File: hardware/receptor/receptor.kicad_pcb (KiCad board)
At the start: 2 copper layers, 100 x 76 mm, 48 parts, among them J1 I2C, J2 USB-C, J3 5V EXT, J4 BOBINA 5V, Q1 AO3400A, SW1 RESET, SW2 BOOT, U1 ESP32-C3-MINI-1-H4X, U2 E220-900T30D, U4 USBLC6-2SC6, U5 AP2112K-3.3

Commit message: feat(hw): layout compacto de 86x52 mm nas duas placas
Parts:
- removed H3, H4: MountingHole_3.2mm_M3, MountingHole:MountingHole_3.2mm_M3
- moved R11 73.0 mm to (80.2, 27.8)
- moved F1 51.6 mm to (75.6, 28.2)
- moved J2 48.7 mm to (14.0, 47.8), turned to 0 degrees
- moved H2 46.5 mm to (82.5, 48.5)
- moved H1 44.5 mm to (3.50, 48.5)
- moved D3 41.4 mm to (68.9, 28.8)
- moved R12 38.3 mm to (45.5, 37.7)
- moved R6 34.0 mm to (30.6, 4.12)
- moved R5 33.9 mm to (26.7, 4.12)
- moved R4 33.8 mm to (22.9, 4.12)
- moved R3 33.6 mm to (19.0, 4.12)
- moved D4 32.4 mm to (60.9, 29.3)
- moved J3 30.6 mm to (48.0, 46.4)
- moved U1 30.4 mm to (11.1, 7.60)
- moved C7 30.2 mm to (30.9, 35.2)
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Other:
- board size 100 x 76 mm -> 86 x 52 mm
- board text added: "ENTRADA 5V APENAS"
- board text added: "FECHADO=BOMBA"
- board text added: "J3: 5V+ | GND"
- board text added: "J4: BOBINA 5V+ | -"
- board text added: "JP1 PAPEL:"
- board text added: "NAO LIGAR 12V"
- board text added: "NAO LIGAR O E220"
- board text added: "RECEPTOR"
- board text added: "SEM ANTENA!"
- board text removed: "BOBINA 5V: + | -"
- board text removed: "ENTRADA 5V APENAS - NAO LIGAR 12V"
- board text removed: "JP1 PAPEL: FECHADO=BOMBA"
- board text removed: "NAO LIGAR O E220 SEM ANTENA!"
- board text removed: "O E220 TRANSMITE NO BOOT"
- board text removed: "RECEPTOR (BOMBA)"

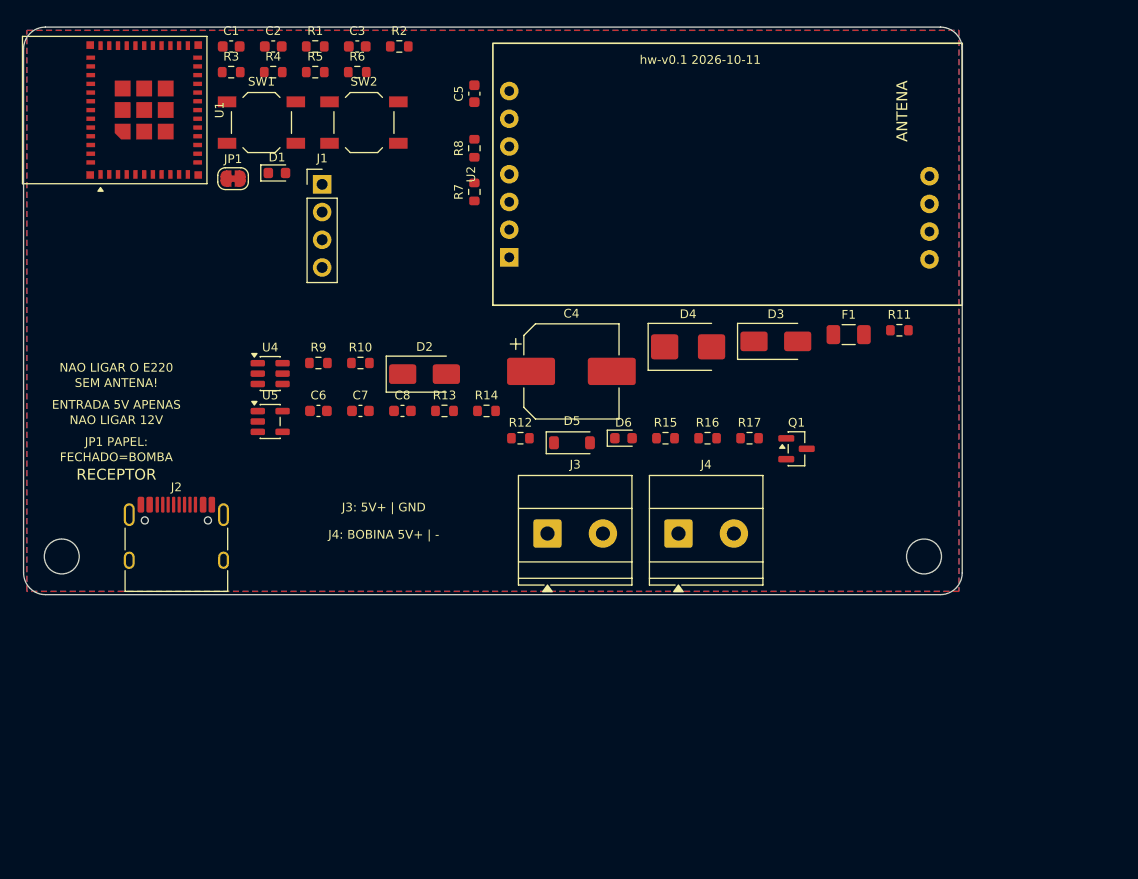
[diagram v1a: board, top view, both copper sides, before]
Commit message: wip(hw): roteador proprio, layout v2 com pecas sob o E220 (checkpoint antes de trocar para jack 12 V)
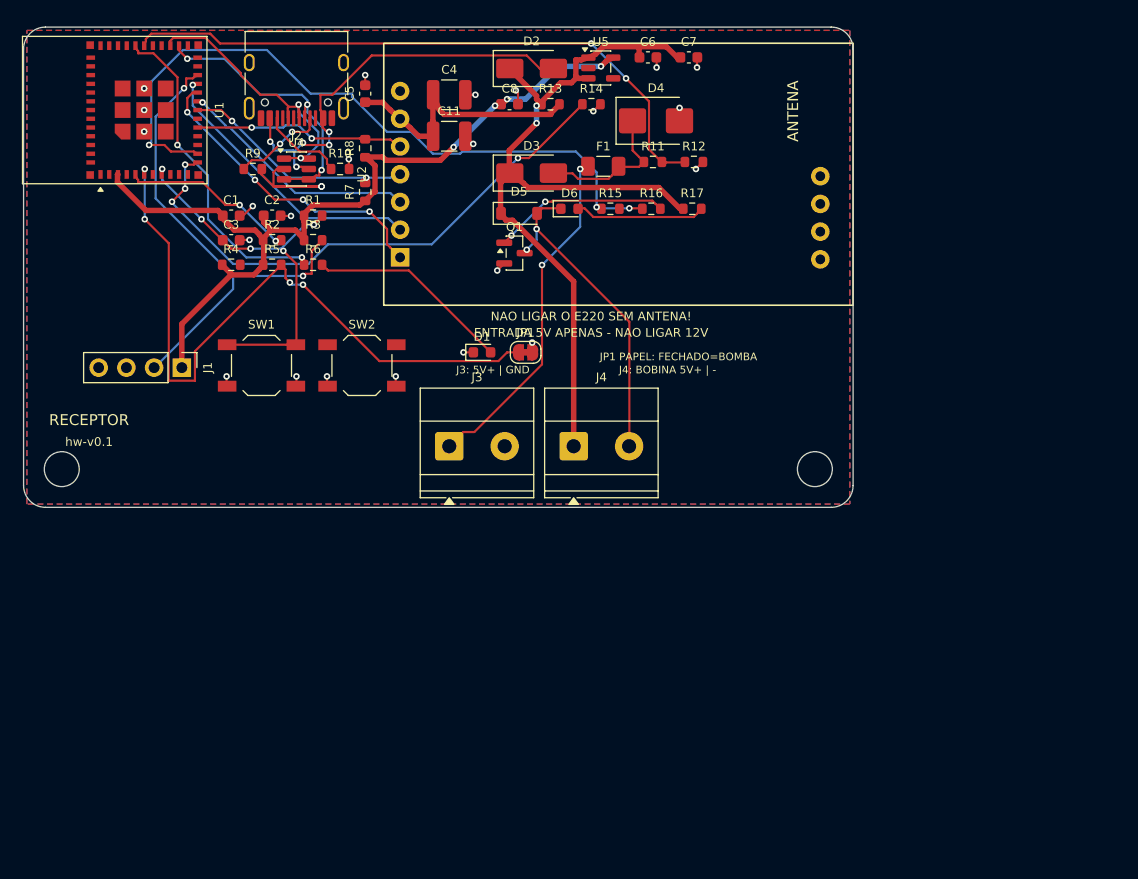
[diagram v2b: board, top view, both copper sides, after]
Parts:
- added C11: 47uF/10V, Capacitor_SMD:C_1210_3225Metric, F.Cu at (39.0, 10.0)
- C4: value 470uF/10V -> 47uF/10V; footprint Capacitor_SMD:CP_Elec_8x10.5 -> Capacitor_SMD:C_1210_3225Metric
- moved J2 44.9 mm to (25.0, 4.30), turned to 180 degrees
- moved U5 44.3 mm to (52.9, 3.75)
- moved C6 44.3 mm to (57.2, 2.77)
- moved C7 44.2 mm to (61.0, 2.77)
- moved Q1 31.5 mm to (45.0, 20.7)
- moved JP1 31.2 mm to (46.0, 29.8)
- moved R12 29.9 mm to (61.4, 12.4)
- moved C8 29.8 mm to (44.5, 7.07)
- moved R13 29.7 mm to (48.3, 7.07)
- moved R14 29.7 mm to (52.0, 7.07)
- moved D2 29.7 mm to (46.5, 3.79)
- moved C4 27.7 mm to (39.0, 6.20)
- moved R11 27.3 mm to (57.7, 12.4)
- moved F1 27.3 mm to (53.1, 12.8)
- moved D3 27.2 mm to (46.5, 13.4)
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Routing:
- net +3V3: track 0.00 -> 80.3 mm, vias 0 -> 4
- net +5V: track 0.00 -> 76.7 mm, vias 0 -> 2
- net PUMP_DRV: track 0.00 -> 65.6 mm, vias 0 -> 3
- net ROLE_STRAP: track 0.00 -> 63.4 mm, vias 0 -> 4
- net EXT_PRESENT: track 0.00 -> 57.8 mm, vias 0 -> 2
- net BAT_ADC: track 0.00 -> 51.2 mm, vias 0 -> 4
- net I2C_SDA: track 0.00 -> 45.6 mm, vias 0 -> 2
- net /Alimentacao/VBUS: track 0.00 -> 40.1 mm, vias 0 -> 5
- net /MCU/MCU_EN: track 0.00 -> 35.9 mm, vias 0 -> 5
- net GND: track 0.00 -> 32.7 mm, vias 0 -> 25
- net /Alimentacao/5V_IN: track 0.00 -> 31.8 mm, vias 0 -> 2
- net LED_STATUS_DRV: track 0.00 -> 30.3 mm, vias 0 -> 2
- net /Entradas e Saidas/COIL_NEG: track 0.00 -> 29.9 mm, vias 0 -> 2
- net E220_M0: track 0.00 -> 28.4 mm, vias 0 -> 4
- net USB_DM: track 0.00 -> 26.5 mm, vias 0 -> 3
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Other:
- board size 86 x 52 mm -> 76 x 44 mm
- board text added: "ENTRADA 5V APENAS - NAO LIGAR 12V"
- board text added: "JP1 PAPEL: FECHADO=BOMBA"
- board text added: "NAO LIGAR O E220 SEM ANTENA!"
- board text added: "hw-v0.1"
- board text removed: "ENTRADA 5V APENAS"
- board text removed: "FECHADO=BOMBA"
- board text removed: "JP1 PAPEL:"
- board text removed: "NAO LIGAR 12V"
- board text removed: "NAO LIGAR O E220"
- board text removed: "SEM ANTENA!"
- board text removed: "hw-v0.1 2026-10-11"

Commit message: feat(hw): jack 12 V com buck AP63205, roteador proprio e serigrafia padronizada (receptor roteado; emissor com 1 net aberta)
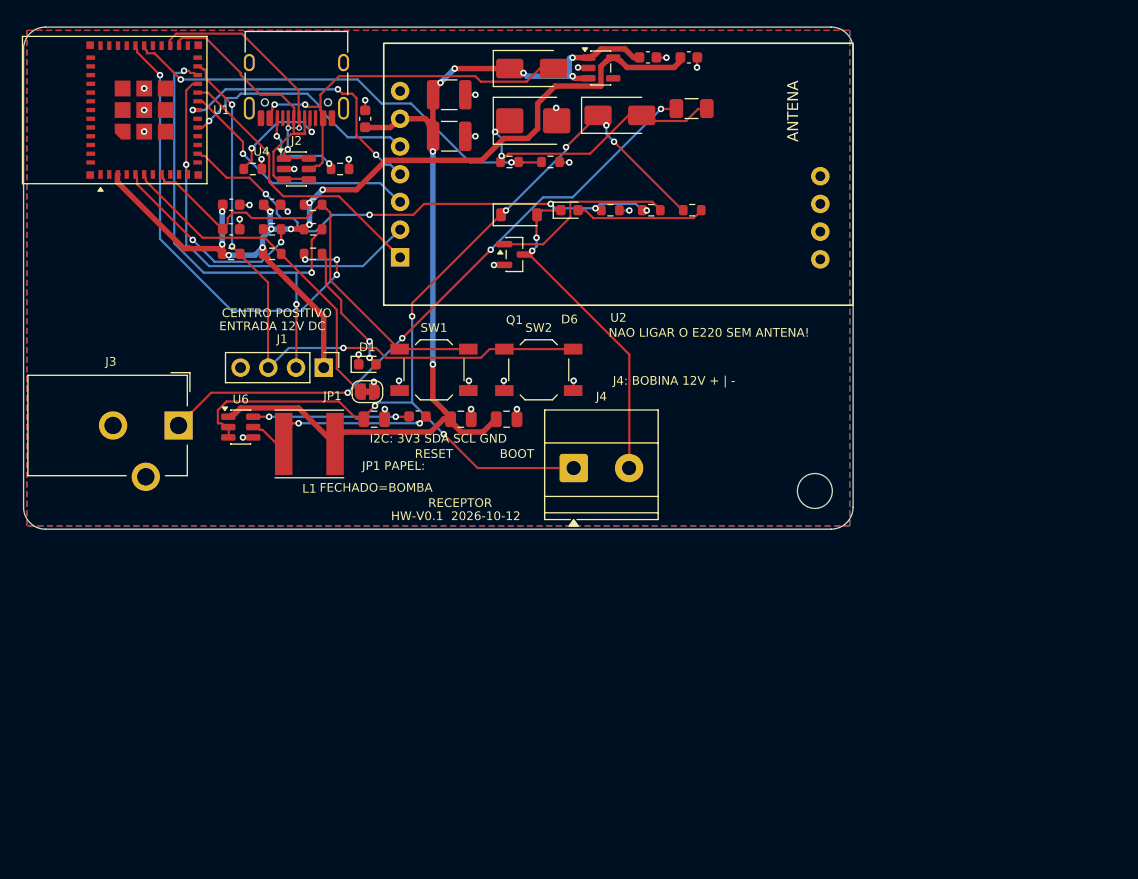
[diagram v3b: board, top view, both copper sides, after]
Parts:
- removed H2: MountingHole_3.2mm_M3, MountingHole:MountingHole_3.2mm_M3
- removed R13: 0R, Resistor_SMD:R_0603_1608Metric
- removed R14: 100k, Resistor_SMD:R_0603_1608Metric
- removed R7, R8: 10k, Resistor_SMD:R_0603_1608Metric
- added C12: 22uF/10V, Capacitor_SMD:C_0805_2012Metric, F.Cu at (40.1, 35.9)
- added C13: 22uF/10V, Capacitor_SMD:C_0805_2012Metric, F.Cu at (44.3, 35.9)
- added C14: 100nF, Capacitor_SMD:C_0603_1608Metric, F.Cu at (36.1, 35.7)
- added L1: 4.7uH, Inductor_SMD:L_Taiyo-Yuden_NR-60xx, F.Cu at (26.2, 38.2)
- added U6: AP63205WU, Package_TO_SOT_SMD:TSOT-23-6, F.Cu at (19.9, 36.6)
- C6: value 10uF -> 10uF/25V; footprint Capacitor_SMD:C_0603_1608Metric -> Capacitor_SMD:C_0805_2012Metric
- D4: value SMBJ5.0A -> SMBJ15A
- F1: value 1.5A -> 1.5A/16V
- J3: value 5V EXT -> JACK 12V; footprint TerminalBlock_Phoenix:TerminalBlock_Phoenix_MKDS-1,5-2-5.08_1x02_P5.08mm_Horizontal -> lora-pump:BarrelJack_CUI_PJ-102AH_Horizontal
- J4: value BOBINA 5V -> BOBINA 12V
- R12: value 100k -> 33k
- R17: value 1k -> 4k7
- moved H1 69.0 mm to (72.5, 42.5)
- moved C6 41.6 mm to (32.1, 35.9)
- moved J3 24.9 mm to (14.2, 36.5), turned to -90 degrees
- moved C8 17.0 mm to (61.0, 2.77)
- moved SW2 16.2 mm to (47.2, 31.4)
- moved SW1 15.8 mm to (37.6, 31.4)
- moved JP1 14.9 mm to (31.5, 33.4)
- moved R11 13.1 mm to (44.5, 12.4)
- moved R12 13.1 mm to (48.3, 12.4)
- moved J1 13.0 mm to (27.5, 31.2)
- moved D4 11.2 mm to (46.7, 8.59)
- moved D1 10.6 mm to (31.5, 30.9)
- moved D3 9.67 mm to (54.6, 8.09)
- moved F1 9.67 mm to (61.2, 7.46)
- moved C7 3.75 mm to (57.2, 2.77)
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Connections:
- net /Alimentacao/+5V_EXT renamed /Alimentacao/+12V_F
- net /Alimentacao/5V_IN renamed /Alimentacao/12V_IN
- C11 pad 1: VCC_RF -> +5V
- C4 pad 1: VCC_RF -> +5V
- C5 pad 1: VCC_RF -> +5V
- C6 pad 1: +5V -> +12V
- D3 pad 1: +5V -> +12V
- D5 pad 1: +5V -> +12V
- J4 pad 1: +5V -> +12V
- R17 pad 1: +5V -> +12V
- U1 pad 12: BAT_ADC -> unconnected-(U1-IO0-Pad12)
- U2 pad 6: VCC_RF -> +5V
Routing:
- net +12V: track 0.00 -> 85.4 mm, vias 0 -> 7
- net I2C_SCL: track 0.00 -> 60.0 mm, vias 0 -> 3
- net BAT_ADC: track 51.2 -> 0.00 mm, vias 4 -> 0
- net ROLE_STRAP: track 63.4 -> 31.5 mm, vias 4 -> 0
- net /Alimentacao/12V_IN: track 31.8 -> 57.6 mm, vias 2 -> 4
- net VCC_RF: track 24.5 -> 0.00 mm
- net PUMP_DRV: track 65.6 -> 47.4 mm, vias 3 -> 5
- net /Alimentacao/SW_BUCK: track 0.00 -> 18.0 mm, vias 0 -> 2
- net EXT_PRESENT: track 57.8 -> 41.2 mm
- net /Alimentacao/BST: track 0.00 -> 14.3 mm, vias 0 -> 2
- net +5V: track 76.7 -> 90.7 mm, vias 2 -> 7
- net LED_STATUS_DRV: track 30.3 -> 43.9 mm, vias 2 -> 4
- net /Alimentacao/+12V_F: track 13.6 -> 26.1 mm, vias 0 -> 2
- net E220_M1: track 26.2 -> 37.4 mm
- net +3V3: track 80.3 -> 89.5 mm, vias 4 -> 10
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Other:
- board size 76 x 44 mm -> 76 x 46 mm
- board text added: "BOOT"
- board text added: "CENTRO POSITIVO"
- board text added: "ENTRADA 12V DC"
- board text added: "FECHADO=BOMBA"
- board text added: "HW-V0.1 2026-10-12"
- board text added: "I2C: 3V3 SDA SCL GND"
- board text added: "J4: BOBINA 12V + | -"
- board text added: "JP1 PAPEL:"
- board text added: "RESET"
- board text removed: "ENTRADA 5V APENAS - NAO LIGAR 12V"
- board text removed: "J3: 5V+ | GND"
- board text removed: "J4: BOBINA 5V+ | -"
- board text removed: "JP1 PAPEL: FECHADO=BOMBA"
- board text removed: "hw-v0.1"
